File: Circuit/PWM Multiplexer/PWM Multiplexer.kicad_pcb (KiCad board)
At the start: 2 copper layers, 63 parts, among them Q1 S8050, Q10 S8050, Q11 S8050, Q12 S8050, Q13 S8050, Q14 S8050, Q2 S8050, Q3 S8050, Q4 S8050, Q5 S8050, Q6 S8050, Q7 S8050, Q8 S8050, Q9 S8050, U1 74HC137, U2 74HC137, U3 L7805

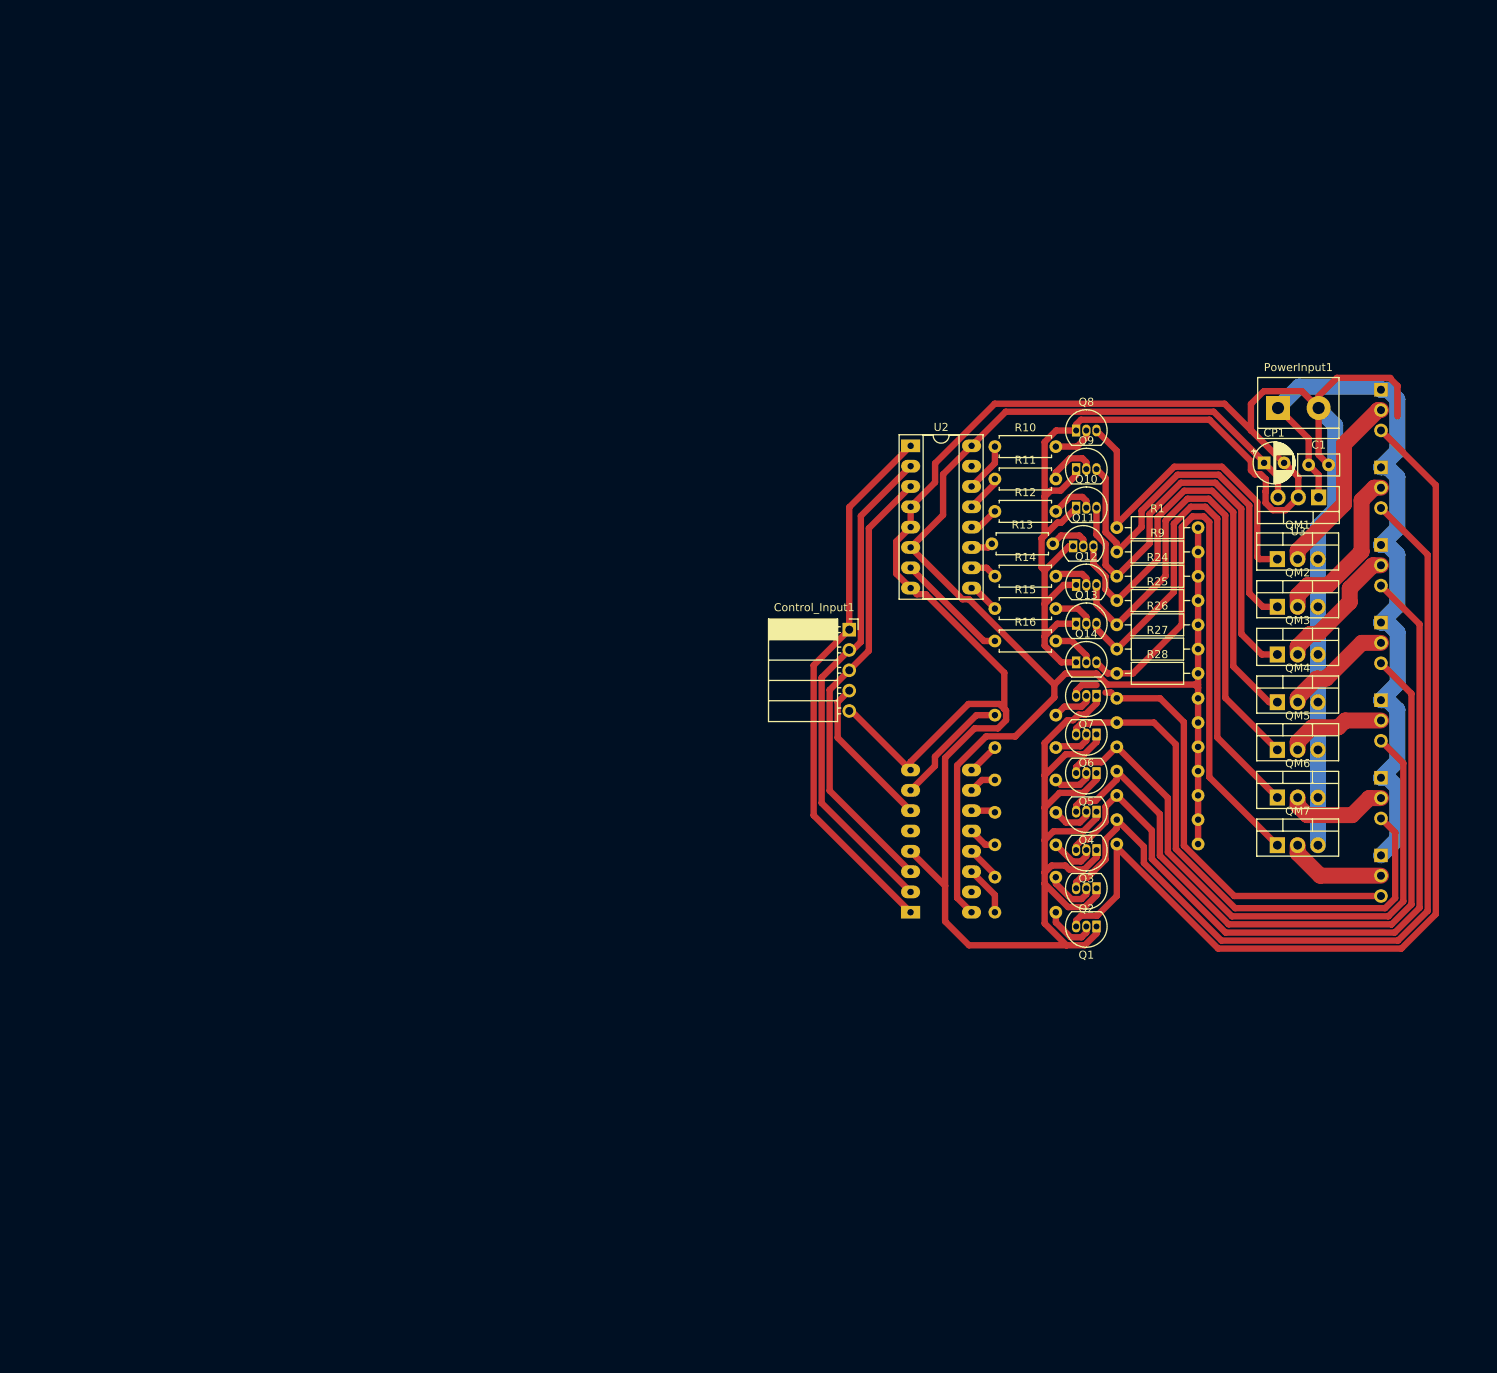
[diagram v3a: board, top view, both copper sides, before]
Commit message: redesigning PWM Multiplexer PCB Solution
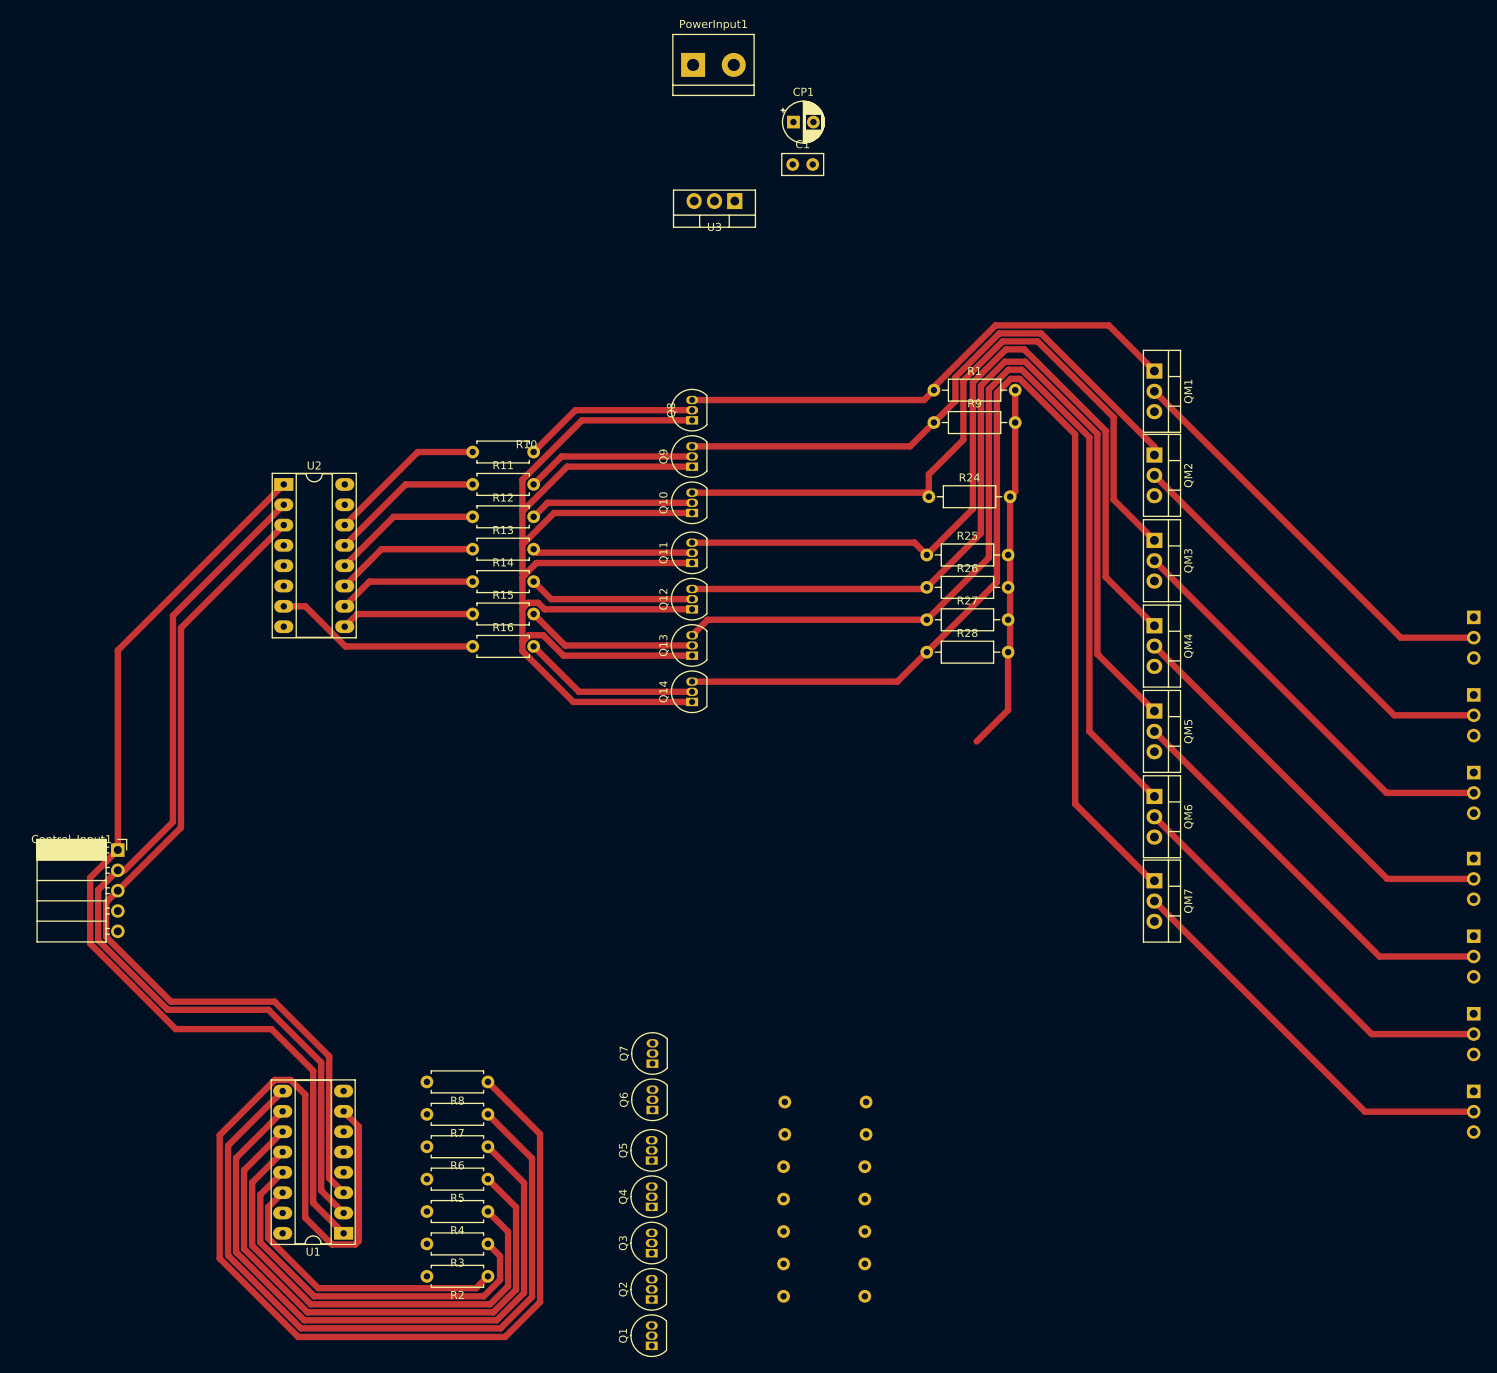
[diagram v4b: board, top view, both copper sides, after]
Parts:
- R2, R3, R4, R5, R6, R7, R8, U1: moved to F.Cu
- moved Control_Input1 95.5 mm to (41.2, 118.5)
- moved PowerInput1 84.8 mm to (113.2, 20.3)
- moved U3 81.8 mm to (118.4, 37.3)
- moved U1 81.4 mm to (69.5, 166.4), turned to 180 degrees
- moved U2 78.5 mm to (62.0, 72.8)
- moved R3 78.2 mm to (87.5, 167.7), turned to 180 degrees
- moved R4 78.2 mm to (87.5, 163.6), turned to 180 degrees
- moved R5 78.2 mm to (87.5, 159.6), turned to 180 degrees
- moved R6 78.2 mm to (87.5, 155.5), turned to 180 degrees
- moved R7 78.2 mm to (87.5, 151.5), turned to 180 degrees
- moved R8 78.2 mm to (87.5, 147.4), turned to 180 degrees
- moved R2 78.0 mm to (87.5, 171.7), turned to 180 degrees
- moved Q1 76.4 mm to (108.0, 180.4), turned to 90 degrees
- moved Q2 75.7 mm to (108.0, 174.6), turned to 90 degrees
- moved Q3 75.0 mm to (108.0, 168.9), turned to 90 degrees
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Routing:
- net GND: track 453.6 -> 182.0 mm
- net +5V: track 182.2 -> 45.9 mm
- net Net-(U1-~{Y7}): track 15.1 -> 146.5 mm
- net D1_PWM: track 124.2 -> 0.00 mm
- net D2_PWM: track 111.8 -> 0.00 mm
- net D3_PWM: track 99.9 -> 0.00 mm
- net +12V: track 98.9 -> 0.00 mm
- net D4_PWM: track 88.8 -> 0.00 mm
- net Net-(U1-~{Y6}): track 4.08 -> 91.9 mm
- net Net-(U1-~{Y5}): track 3.46 -> 81.1 mm
- net D5_PWM: track 77.4 -> 0.00 mm
- net D6_PWM: track 69.4 -> 0.00 mm
- net Net-(U1-~{Y4}): track 3.01 -> 70.4 mm
- net Net-(Q14-C): track 74.2 -> 140.4 mm
- net Net-(Q13-C): track 67.7 -> 127.5 mm
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
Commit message: Further development in PWM Multiplexer PCB solution
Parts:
- Q1, Q2, Q3, Q4, Q5, Q6, Q7: moved to B.Cu
- R17, R18, R19, R20, R21, R22, R23: moved to F.Cu
- moved Q1 37.3 mm to (108.7, 143.2), turned to -90 degrees
- moved Q7 33.3 mm to (108.8, 178.4), turned to -90 degrees
- moved R8 28.1 mm to (79.9, 174.5), turned to 0 degrees
- moved R23 27.0 mm to (124.5, 177.0)
- moved Q2 25.7 mm to (108.7, 148.9), turned to -90 degrees
- moved R2 22.9 mm to (79.9, 150.2), turned to 0 degrees
- moved Q6 21.7 mm to (108.8, 172.6), turned to -90 degrees
- moved R17 21.6 mm to (124.3, 152.7)
- moved R7 20.4 mm to (79.9, 170.4), turned to 0 degrees
- moved U1 19.3 mm to (59.3, 150.0), turned to 0 degrees
- moved R22 18.9 mm to (124.5, 172.9)
- moved R3 15.5 mm to (79.9, 154.2), turned to 0 degrees
- moved Q3 14.1 mm to (108.7, 154.7), turned to -90 degrees
- moved R18 13.5 mm to (124.3, 156.7)
- moved R6 13.3 mm to (79.9, 166.4), turned to 0 degrees
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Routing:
- net D1_PWM: track 0.00 -> 450.5 mm
- net D2_PWM: track 0.00 -> 403.0 mm
- net D3_PWM: track 0.00 -> 338.1 mm
- net D4_PWM: track 0.00 -> 293.8 mm
- net D5_PWM: track 0.00 -> 254.6 mm
- net GND: track 182.0 -> 421.1 mm
- net D6_PWM: track 0.00 -> 230.1 mm
- net D7_PWM: track 0.00 -> 130.6 mm
- net Net-(U1-~{Y7}): track 146.5 -> 24.5 mm
- net Net-(U1-~{Y6}): track 91.9 -> 14.1 mm
- net +12V: track 0.00 -> 77.1 mm
- net Net-(U1-~{Y5}): track 81.1 -> 13.4 mm
- net Net-(U1-~{Y4}): track 70.4 -> 13.1 mm
- net Net-(U1-~{Y3}): track 59.6 -> 13.7 mm
- net Net-(U1-~{Y2}): track 48.7 -> 14.4 mm
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
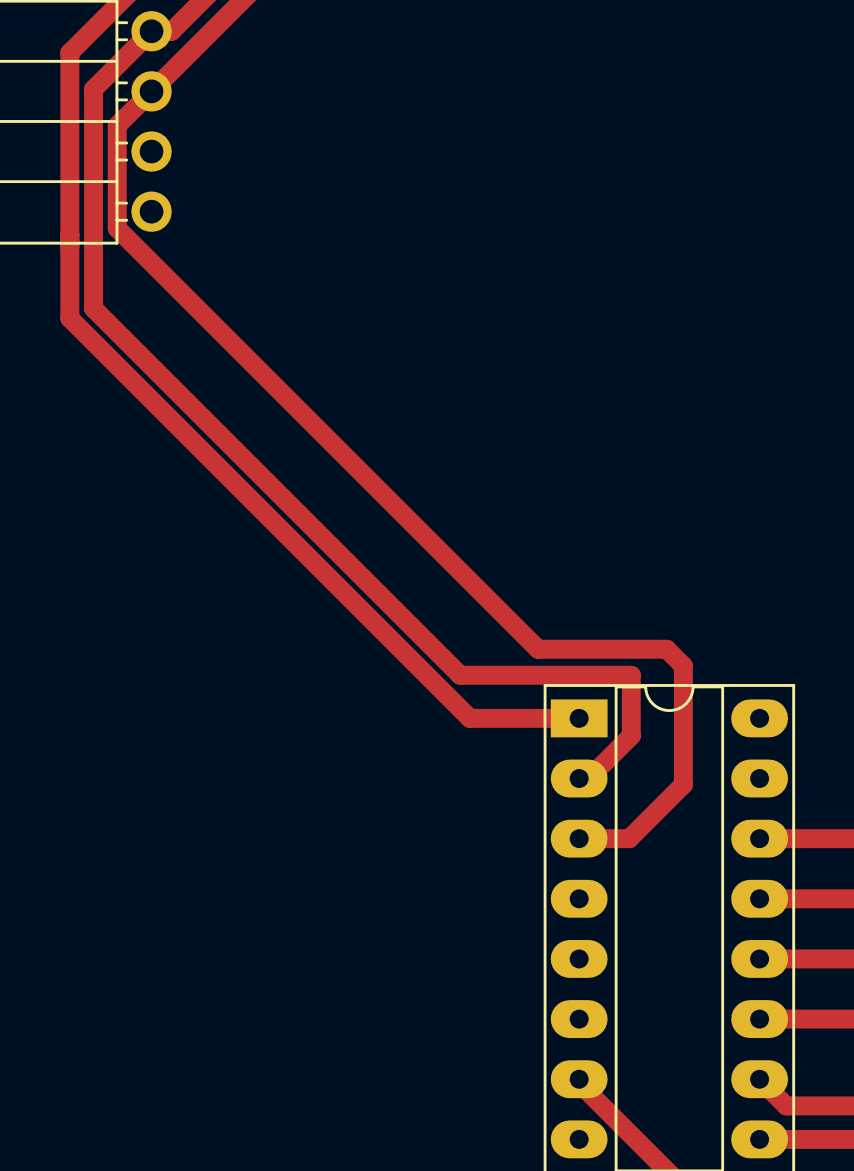
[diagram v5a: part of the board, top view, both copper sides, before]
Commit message: Implemented Isolators in PWM Mutliplexer
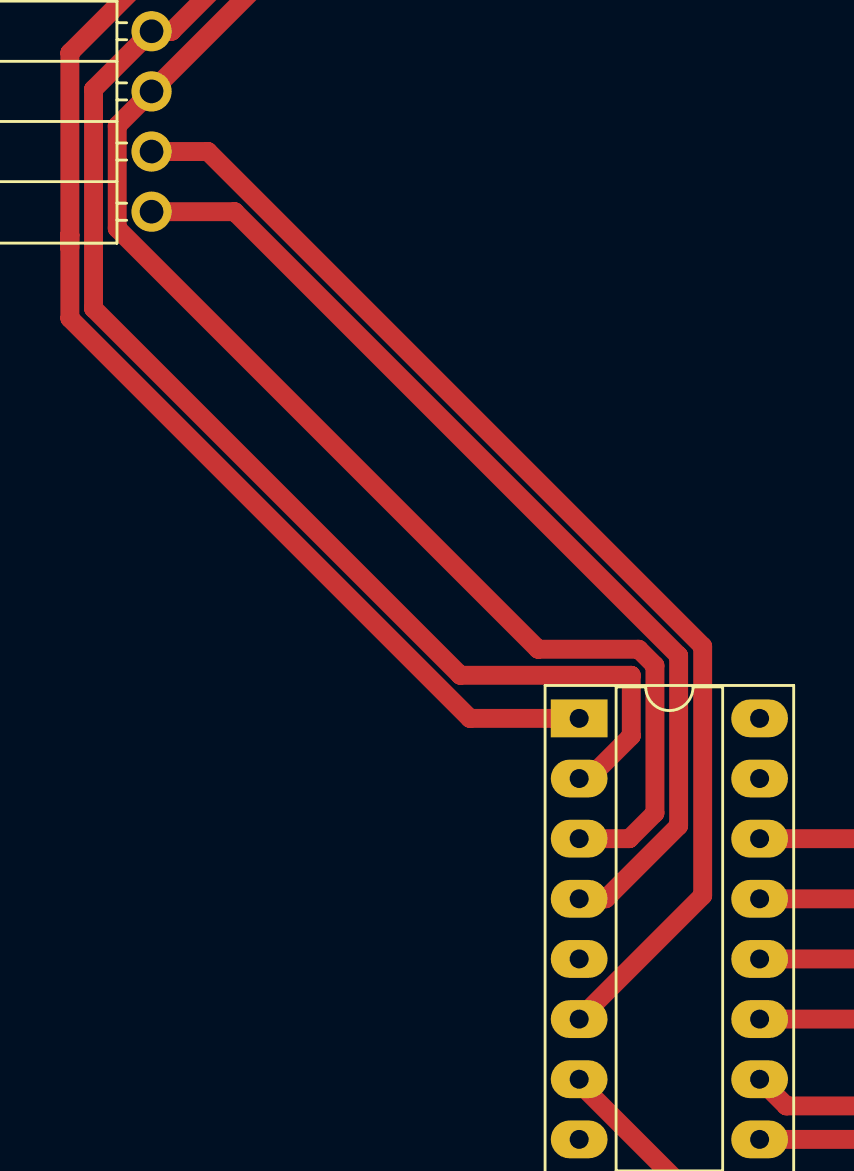
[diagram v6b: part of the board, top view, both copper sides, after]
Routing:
- net PWM: track 0.00 -> 49.8 mm
- net GND: track 421.1 -> 463.8 mm
- net A2: track 102.6 -> 100.9 mm
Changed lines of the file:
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@@
   (segment (start 212.8 127.156) (end 212.8 136.856) (width 2) (layer "B.Cu") (net 1))
   (segment (start 94.602786 88.369) (end 93.790786 87.557) (width 0.8) (layer "F.Cu") (net 2))
+  (segment (start 63.5 147.371572) (end 63.5 154.559) (width 0.8) (layer "F.Cu") (net 2))
   (segment (start 125.86 173.498899) (end 125.86 172.339101) (width 0.8) (layer "F.Cu") (net 2))
   (segment (start 113.03 88.369) (end 94.602786 88.369) (width 0.8) (layer "F.Cu") (net 2))
@@
   (segment (start 93.790786 87.557) (end 92.529 87.557) (width 0.8) (layer "F.Cu") (net 2))
   (segment (start 91.818 88.268) (end 91.818 92.434214) (width 0.8) (layer "F.Cu") (net 2))
+  (segment (start 60.419 157.64) (end 59.3 157.64) (width 0.8) (layer "F.Cu") (net 2))
   (segment (start 92.075 88.011) (end 91.818 88.268) (width 0.8) (layer "F.Cu") (net 2))
   (segment (start 93.573214 82.579) (end 113.03 82.579) (width 0.8) (layer "F.Cu") (net 2))
@@
   (segment (start 125.86 172.339101) (end 125.51045 171.98955) (width 0.8) (layer "F.Cu") (net 2))
   (segment (start 123.805101 166.316) (end 108.659 166.316) (width 0.8) (layer "F.Cu") (net 2))
+  (segment (start 63.5 154.559) (end 60.419 157.64) (width 0.8) (layer "F.Cu") (net 2))
   (segment (start 125.703 164.254101) (end 123.248899 161.8) (width 0.8) (layer "F.Cu") (net 2))
   (segment (start 108.753 178.431) (end 120.927899 178.431) (width 0.8) (layer "F.Cu") (net 2))
   (segment (start 98.187214 99.949) (end 91.818 93.579786) (width 0.8) (layer "F.Cu") (net 2))
+  (segment (start 44.749428 128.621) (end 63.5 147.371572) (width 0.8) (layer "F.Cu") (net 2))
   (segment (start 125.703 168.213899) (end 125.703 164.254101) (width 0.8) (layer "F.Cu") (net 2))
   (segment (start 118.585101 148.946) (end 125.703 156.063899) (width 0.8) (layer "F.Cu") (net 2))
@@
   (segment (start 125.703 156.063899) (end 125.703 152.104101) (width 0.8) (layer "F.Cu") (net 2))
   (segment (start 125.703 160.204101) (end 120.234899 154.736) (width 0.8) (layer "F.Cu") (net 2))
+  (segment (start 41.24 128.621) (end 44.749428 128.621) (width 0.8) (layer "F.Cu") (net 2))
   (segment (start 170.815 74.168) (end 173.015 76.368) (width 2) (layer "B.Cu") (net 2))
   (segment (start 173.015 119.04) (end 173.015 110) (width 2) (layer "B.Cu") (net 2))
@@
   (segment (start 173.015 119.04) (end 170.815 116.84) (width 2) (layer "B.Cu") (net 2))
   (segment (start 170.815 127.381) (end 171.366595 127.381) (width 2) (layer "B.Cu") (net 2))
+  (segment (start 43.623642 126.081) (end 64.516 146.973358) (width 0.8) (layer "F.Cu") (net 3))
+  (segment (start 64.516 157.504) (end 59.3 162.72) (width 0.8) (layer "F.Cu") (net 3))
+  (segment (start 64.516 146.973358) (end 64.516 157.504) (width 0.8) (layer "F.Cu") (net 3))
+  (segment (start 41.24 126.081) (end 43.623642 126.081) (width 0.8) (layer "F.Cu") (net 3))
   (segment (start 39.79 129.325) (end 57.565 147.1) (width 0.8) (layer "F.Cu") (net 4))
   (segment (start 39.79 124.991) (end 39.79 129.325) (width 0.8) (layer "F.Cu") (net 4))
   (segment (start 61.419899 155.1) (end 59.3 155.1) (width 0.8) (layer "F.Cu") (net 4))
   (segment (start 49.133 115.648) (end 41.24 123.541) (width 0.8) (layer "F.Cu") (net 4))
-  (segment (start 63.7 147.8) (end 63.7 152.819899) (width 0.8) (layer "F.Cu") (net 4))
-  (segment (start 57.565 147.1) (end 63 147.1) (width 0.8) (layer "F.Cu") (net 4))
-  (segment (start 63.7 152.819899) (end 61.419899 155.1) (width 0.8) (layer "F.Cu") (net 4))
-  (segment (start 63 147.1) (end 63.7 147.8) (width 0.8) (layer "F.Cu") (net 4))
   (segment (start 49.133 90.694) (end 49.133 115.648) (width 0.8) (layer "F.Cu") (net 4))
   (segment (start 61.986 77.841) (end 49.133 90.694) (width 0.8) (layer "F.Cu") (net 4))
+  (segment (start 57.565 147.1) (end 61.814214 147.1) (width 0.8) (layer "F.Cu") (net 4))
+  (segment (start 62.5 147.785786) (end 62.5 154.019899) (width 0.8) (layer "F.Cu") (net 4))
+  (segment (start 62.5 154.019899) (end 61.419899 155.1) (width 0.8) (layer "F.Cu") (net 4))
+  (segment (start 61.814214 147.1) (end 62.5 147.785786) (width 0.8) (layer "F.Cu") (net 4))
   (segment (start 41.24 123.541) (end 39.79 124.991) (width 0.8) (layer "F.Cu") (net 4))
   (segment (start 61.5 148.2) (end 61.5 150.76) (width 0.8) (layer "F.Cu") (net 5))
